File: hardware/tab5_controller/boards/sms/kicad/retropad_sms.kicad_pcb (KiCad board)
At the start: 2 copper layers, 125 x 55 mm, 36 parts, among them J1 Tab5 Ext.Port1, J2 SWD, SW1 UP, SW2 DOWN, SW3 LEFT, SW4 RIGHT, SW5 1, SW6 2, SW7 START, SW8 MENU, U1 STM32F030C8T6

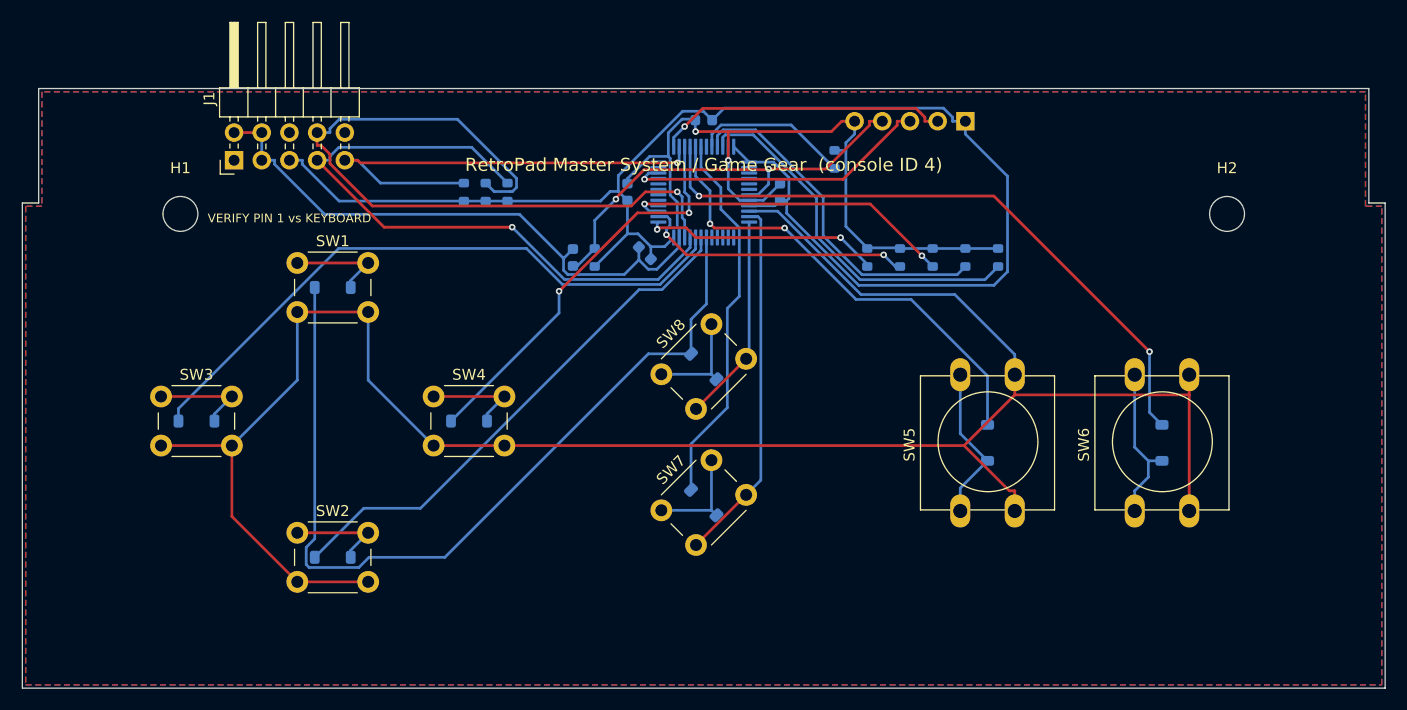
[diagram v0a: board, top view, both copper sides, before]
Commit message: tab5_controller: build every console board on the AVR32DD28
The STM32F030 matrix boards are gone. SNES, NES, Game Boy, Genesis and
Master System / Game Gear are now all AVR32DD28 boards: one MCU pin per
button, no diodes, UPDI programming, one firmware image (firmware_avrdd)
keyed by the console-ID straps.

- layout.py / gen_pcb.py / gen_sch.py: drop the stm32 core (LQFP-48,
  key matrix, diodes, SWD header, AN_EN strap); the AVR DD core is the
  only one, and the *_dd board names become the plain console names.
- SNES, NES and Genesis keep the routing of their AVR DD prototypes;
  Game Boy and Master System are routed fresh.
- Every board: DRC 0 unconnected (silkscreen warnings only), schematic
  vs PCB 0 differences, and each switch checked against the MCU pin
  pinmap.h gives it for that console ID.
- Host test now also covers the Game Boy and Master System pin maps.
- READMEs describe the AVR DD boards only.

Co-Authored-By: Claude Opus 5.5 <noreply@anthropic.com>
Claude-Session: https://claude.ai/code/session_01NhSHTsezreiVZCnuBhQzP2
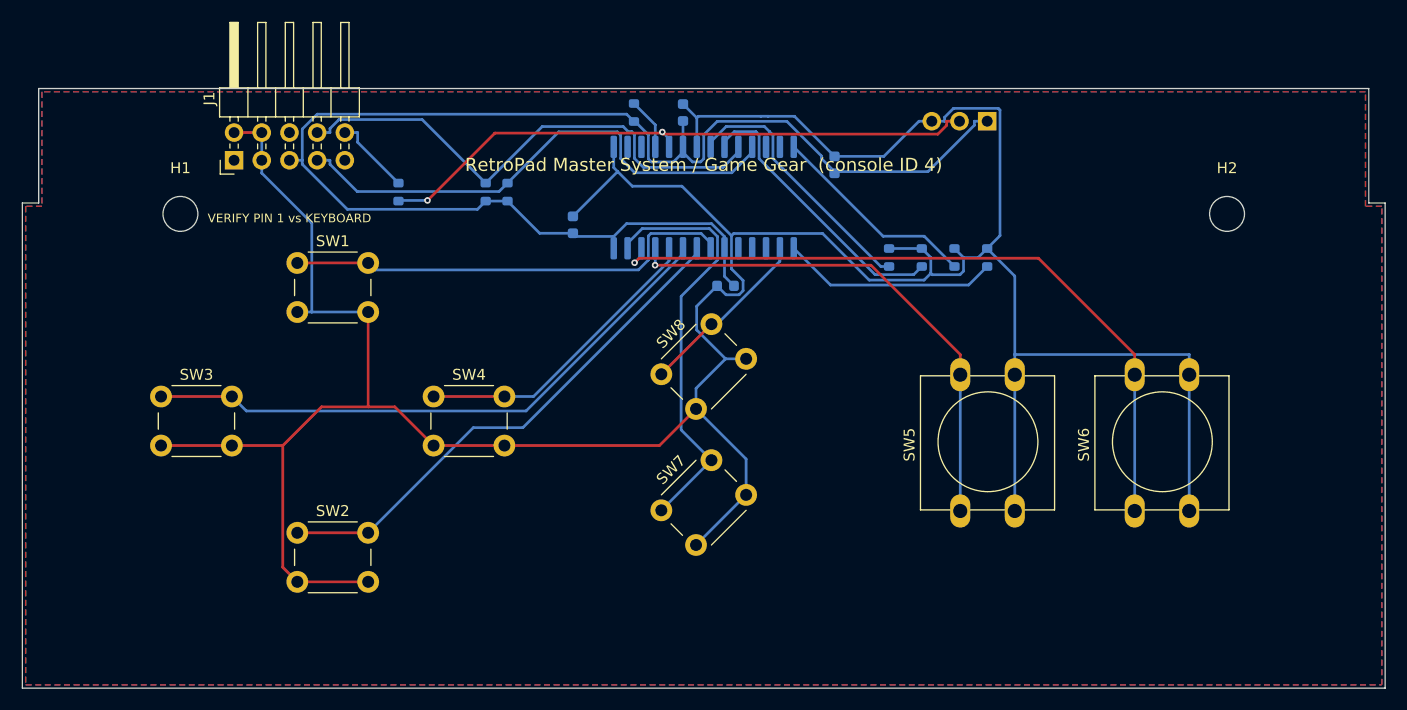
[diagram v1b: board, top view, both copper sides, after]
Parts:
- removed C5: 100nF, Capacitor_SMD:C_0603_1608Metric
- removed D1, D2, D3, D4, D5, D6, D7, D8: 1N4148W, Diode_SMD:D_SOD-123
- removed R10: DNP, Resistor_SMD:R_0603_1608Metric
- removed R4, R5: 10k, Resistor_SMD:R_0603_1608Metric
- added R11: DNP, Resistor_SMD:R_0603_1608Metric, B.Cu at (76.0, 93.0)
- J2: value SWD -> UPDI; footprint Connector_PinHeader_2.54mm:PinHeader_1x05_P2.54mm_Vertical -> Connector_PinHeader_2.54mm:PinHeader_1x03_P2.54mm_Vertical
- U1: value STM32F030C8T6 -> AVR32DD28-I/SO; footprint Package_QFP:LQFP-48_7x7mm_P0.5mm -> Package_SO:SOIC-28W_7.5x17.9mm_P1.27mm
- moved R3 17.2 mm to (97.6, 85.7)
- moved C4 12.7 mm to (116.0, 90.5), turned to 90 degrees
- moved C2 11.5 mm to (102.1, 85.7)
- moved C3 7.98 mm to (106.0, 101.6), turned to 180 degrees
- moved C1 5.83 mm to (92.0, 96.0)
- moved J2 2.00 mm to (130.0, 86.5)
- moved R6 2.00 mm to (121.0, 99.0)
- moved R7 2.00 mm to (124.0, 99.0)
- moved R8 2.00 mm to (127.0, 99.0)
- moved R9 2.00 mm to (130.0, 99.0)
- moved U1 0.50 mm to (104.0, 93.5), turned to 90 degrees
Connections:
- J1 pad 10: (no net) -> G9_UPDI
- J1 pad 9: INT -> (no net)
- J2 pad 2: SWCLK -> UPDI
- J2 pad 3: SWDIO -> GND
- R3 pad 2: INT -> RESET
- SW1 pad 2: COL0 -> GND
- SW2 pad 2: COL0 -> GND
- SW3 pad 2: COL0 -> GND
- SW4 pad 2: COL0 -> GND
- SW5 pad 2: COL0 -> GND
- SW6 pad 2: COL0 -> GND
- SW7 pad 2: COL1 -> GND
- SW8 pad 2: COL2 -> GND
- U1 pad 1: +3V3 -> ID3
- U1 pad 10: COL0 -> K_RIGHT
- U1 pad 11: COL1 -> K_1
- U1 pad 12: COL2 -> K_2
- U1 pad 13: COL3 -> K_START
- U1 pad 14: (no net) -> +3V3
- U1 pad 15: (no net) -> GND
- U1 pad 18: ROW0 -> RESET
- U1 pad 19: ROW1 -> UPDI
- U1 pad 2: (no net) -> K_MENU
- U1 pad 20: ROW2 -> +3V3
- U1 pad 21: SCL -> GND
- U1 pad 22: SDA -> ID0
- U1 pad 23: GND -> ID1
- U1 pad 24: +3V3 -> SDA
- U1 pad 25: ID0 -> SCL
- U1 pad 26: ID1 -> AN0
- U1 pad 27: ID2 -> AN1
- U1 pad 28: (no net) -> ID2
- U1 pad 6: (no net) -> +3V3
- U1 pad 7: NRST -> K_UP
- U1 pad 8: GND -> K_DOWN
- U1 pad 9: +3V3 -> K_LEFT
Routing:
- net COL0: track 189.4 -> 0.00 mm
- net GND: track 125.9 -> 309.7 mm, vias 2 -> 0
- net ROW0: track 80.5 -> 0.00 mm
- net ROW4: track 59.3 -> 0.00 mm, vias 2 -> 0
- net ROW2: track 58.4 -> 0.00 mm
- net UPDI: track 0.00 -> 56.5 mm, vias 0 -> 2
- net K_2: track 14.8 -> 65.6 mm, vias 0 -> 1
- net ROW1: track 48.3 -> 0.00 mm
- net K_LEFT: track 9.41 -> 54.9 mm
- net INT: track 43.9 -> 0.00 mm, vias 1 -> 0
- net ROW5: track 43.3 -> 0.00 mm, vias 2 -> 0
- net NRST: track 39.3 -> 0.00 mm, vias 2 -> 0
- net K_DOWN: track 9.41 -> 47.7 mm
- net ROW3: track 37.1 -> 0.00 mm, vias 2 -> 0
- net ROW6: track 34.8 -> 0.00 mm
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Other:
- board text added: "ID0 ID1 ID2 ID3"
- board text added: "UPDI 3V3 UPDI GND"
- board text removed: "ID0 ID1 ID2 ID3 AN"
- board text removed: "SWD 3V3 CLK DIO RST GND"

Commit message: tab5_controller: remove the UPDI-to-G9 link (R11) from every board
The Tab5 never updates controller firmware, so J1 pin 10 (G9) is left
unconnected, as on M5Stack's keyboard, and R11 and the G9_UPDI net are
gone. Boards are programmed only through their own UPDI header J2.

All five boards are re-routed (the old routes ended at R11). Game Boy
is routed with Freerouting 2.1 single-threaded because 1.9 stalls with
UPDI unrouted on it. Every board: DRC 0 unconnected pads (silkscreen
warnings only), schematic vs PCB 0 differences, switches on the pins
pinmap.h expects.

Co-Authored-By: Claude Opus 5.5 <noreply@anthropic.com>
Claude-Session: https://claude.ai/code/session_01NhSHTsezreiVZCnuBhQzP2
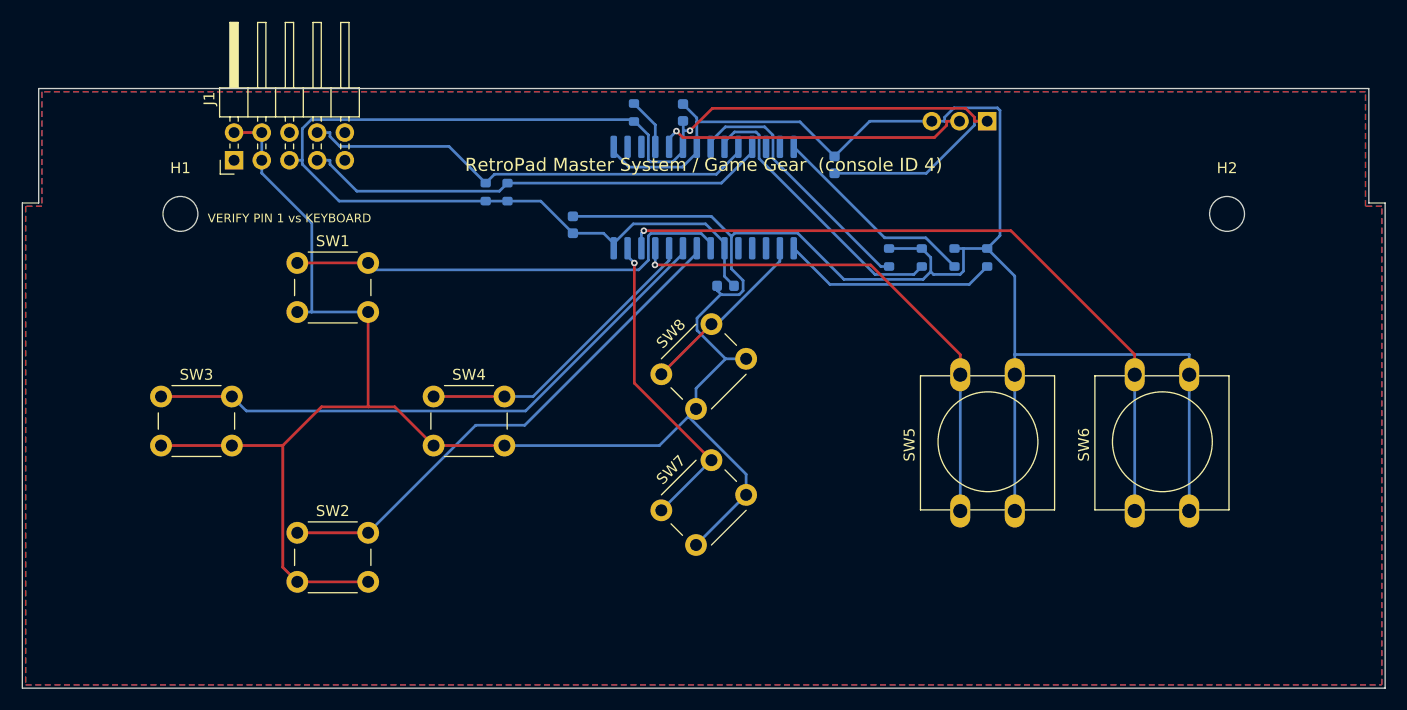
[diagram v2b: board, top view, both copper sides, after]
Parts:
- removed R11: DNP, Resistor_SMD:R_0603_1608Metric
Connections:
- J1 pad 10: G9_UPDI -> (no net)
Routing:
- net UPDI: track 56.5 -> 28.8 mm, vias 2 -> 1
- net K_START: track 39.1 -> 29.1 mm, vias 0 -> 1
- net +3V3: track 130.7 -> 139.4 mm, vias 0 -> 1
- net G9_UPDI: track 7.36 -> 0.00 mm
- net SDA: track 47.8 -> 42.4 mm
- net SCL: track 47.7 -> 43.3 mm
- net GND: track 309.7 -> 312.6 mm

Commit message: tab5_controller: 0805 hand-solder passives on every board
Swap the 0603 resistors and capacitors (decoupling, I2C pull-ups, reset
pull-up, console-ID straps) for KiCad's 0805 HandSolder footprints, which
have longer pads for soldering by hand. C2 turns 90 degrees so its larger
courtyard clears U1. All four boards are re-routed with Freerouting 1.9;
schematics, BOMs, DRC reports and renders are regenerated.

DRC: 0 errors and 0 unconnected pads on every board (silkscreen and
library-path warnings only). Schematic vs PCB: 0 differences.

Co-Authored-By: Claude Opus 5.5 <noreply@anthropic.com>
Claude-Session: https://claude.ai/code/session_016pgTnJvu7Wh4anaUwDfFmN
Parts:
- C1, C2, C3, C4: footprint Capacitor_SMD:C_0603_1608Metric -> Capacitor_SMD:C_0805_2012Metric_Pad1.18x1.45mm_HandSolder
- R1, R2, R3, R6, R7, R8, R9: footprint Resistor_SMD:R_0603_1608Metric -> Resistor_SMD:R_0805_2012Metric_Pad1.20x1.40mm_HandSolder
- turned C2 to 180 degrees
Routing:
- net K_UP: track 41.7 -> 53.6 mm
- net K_START: track 29.1 -> 40.9 mm, vias 1 -> 0
- net GND: track 312.6 -> 320.5 mm, vias 0 -> 1
- net RESET: track 4.78 -> 11.8 mm
- net +3V3: track 139.4 -> 142.4 mm, vias 1 -> 0
- net UPDI: track 28.8 -> 31.5 mm, vias 1 -> 0
- net K_2: track 65.8 -> 64.2 mm
- net ID2: track 19.3 -> 20.5 mm
- net K_LEFT: track 54.9 -> 55.9 mm
- net K_MENU: track 16.4 -> 16.1 mm, vias 0 -> 1

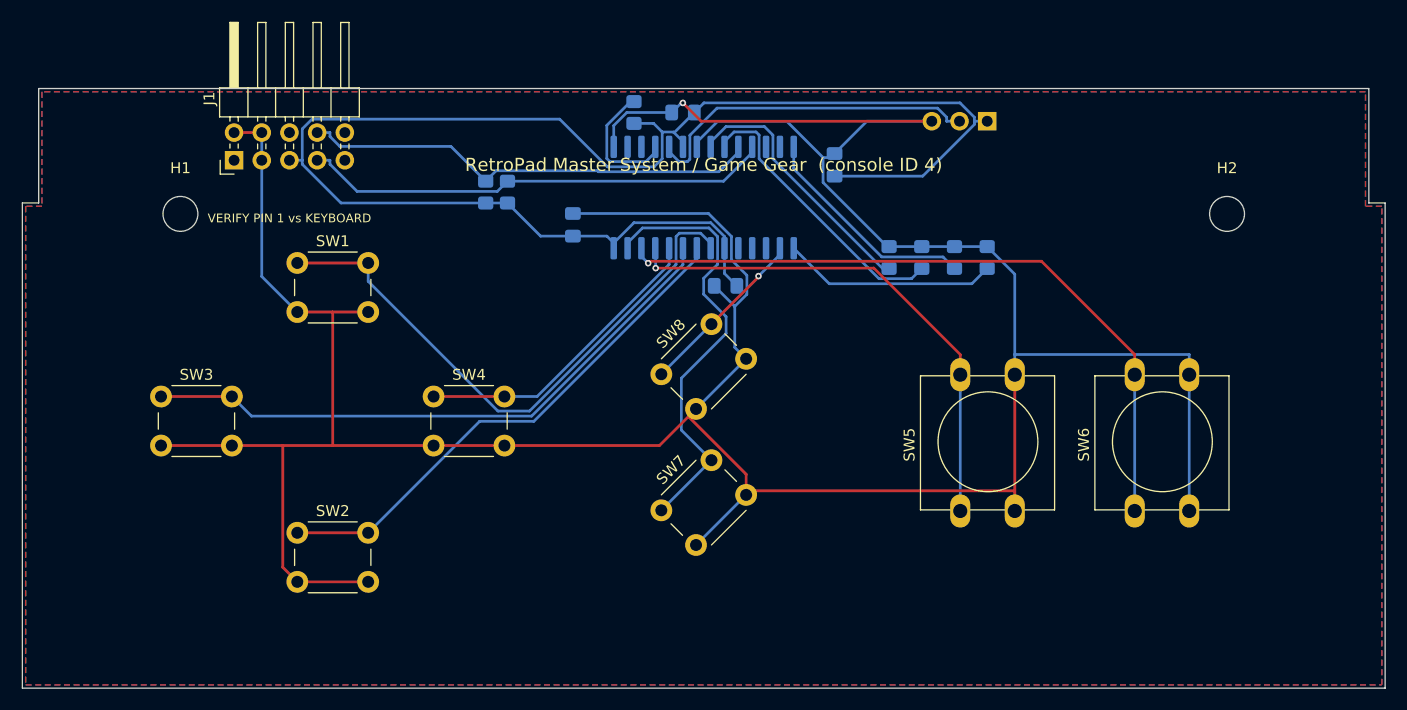
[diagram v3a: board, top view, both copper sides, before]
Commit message: tab5_controller: 4-pin tact switch symbols and footprints
The 6x6 and 12x12 switches are 4-leg parts, and the production layout in
EasyEDA uses their 4-pin symbols, so the KiCad boards now match:

- kicad_lib/RetroPad.pretty: SW_PUSH_6mm_4pin and SW_PUSH-12mm_4pin,
  KiCad's footprints with the pads renumbered 1-4 (pad 1 top-left, then
  clockwise; tied pairs 1-2 and 3-4, the legs 6.5 / 12.5 mm apart).
  gen_pcb.py writes them from the stock footprints and points each
  board's fp-lib-table at the library.
- RetroPad:SW_Push_4pin symbol in gen_sch.py: 1-2 tied, 4-3 tied, one
  contact between. KiCad's 4-pin SW_Push_Dual is a two-contact switch,
  so it doesn't fit these parts.
- Wiring: legs 1-2 to GND, 3-4 to K_<button>. L/R (right angle, two
  contacts plus mounting legs) keep the 2-pin SW_Push.
- All four boards re-routed: DRC 0 unconnected (silkscreen warnings
  only), schematic vs PCB 0 differences, every switch on the pin
  pinmap.h expects; firmware host test passes; Gerber/drill export OK.

Co-Authored-By: Claude Opus 5.5 <noreply@anthropic.com>
Claude-Session: https://claude.ai/code/session_01NhSHTsezreiVZCnuBhQzP2
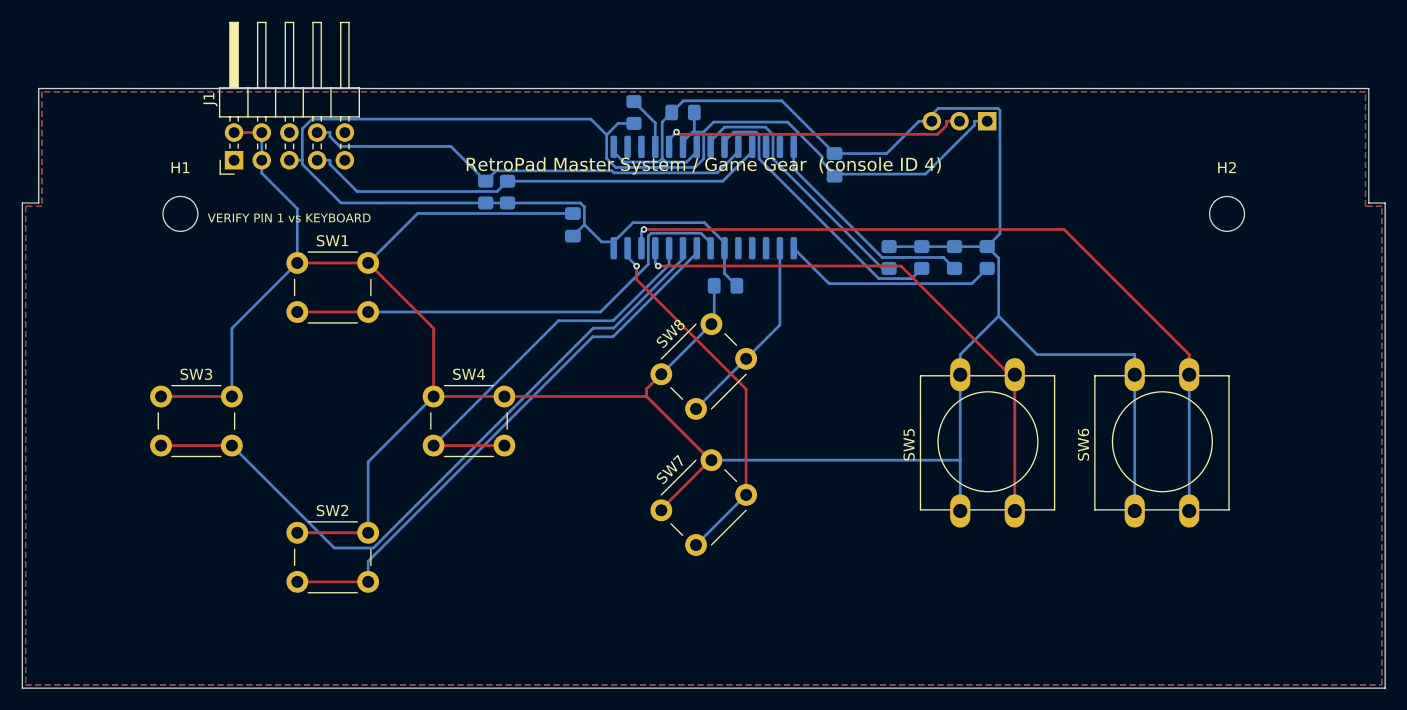
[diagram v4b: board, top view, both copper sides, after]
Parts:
- SW1, SW2, SW3, SW4, SW7, SW8: footprint Button_Switch_THT:SW_PUSH_6mm -> RetroPad:SW_PUSH_6mm_4pin
- SW5, SW6: footprint Button_Switch_THT:SW_PUSH-12mm -> RetroPad:SW_PUSH-12mm_4pin
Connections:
- SW1 pad 1: K_UP -> GND
- SW2 pad 1: K_DOWN -> GND
- SW3 pad 1: K_LEFT -> GND
- SW4 pad 1: K_RIGHT -> GND
- SW5 pad 1: K_1 -> GND
- SW6 pad 1: K_2 -> GND
- SW7 pad 1: K_START -> GND
- SW8 pad 1: K_MENU -> GND
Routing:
- net GND: track 320.5 -> 295.9 mm, vias 1 -> 0
- net K_UP: track 53.6 -> 43.3 mm
- net K_RIGHT: track 28.1 -> 36.5 mm
- net K_LEFT: track 55.9 -> 63.7 mm
- net K_START: track 40.9 -> 33.6 mm, vias 0 -> 1
- net RESET: track 11.8 -> 4.96 mm
- net K_2: track 64.2 -> 70.9 mm
- net +3V3: track 142.4 -> 136.6 mm
- net K_1: track 47.4 -> 51.3 mm
- net UPDI: track 31.5 -> 28.4 mm, vias 0 -> 1
- net K_DOWN: track 48.0 -> 50.7 mm
- net K_MENU: track 16.1 -> 17.9 mm, vias 1 -> 0

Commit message: tab5_controller: label each console-ID strap under its own resistor
The back silkscreen printed one mirrored "ID0 ID1 ID2 ID3" string, which
reads left to right from the back while the straps appear right to left
(R9/ID3 first), so the labels were in the reverse order of the parts.
Each strap now gets its own ID<n> label centred under it. Silkscreen
only: the boards keep their routing (same segments and vias), DRC 0
unconnected, schematic vs PCB 0 differences.

Co-Authored-By: Claude Opus 5.5 <noreply@anthropic.com>
Claude-Session: https://claude.ai/code/session_01NhSHTsezreiVZCnuBhQzP2
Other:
- board text added: "ID0"
- board text added: "ID1"
- board text added: "ID2"
- board text added: "ID3"
- board text removed: "ID0 ID1 ID2 ID3"
